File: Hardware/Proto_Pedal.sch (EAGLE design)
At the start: 124 parts, among them Q1 2.5A/30V

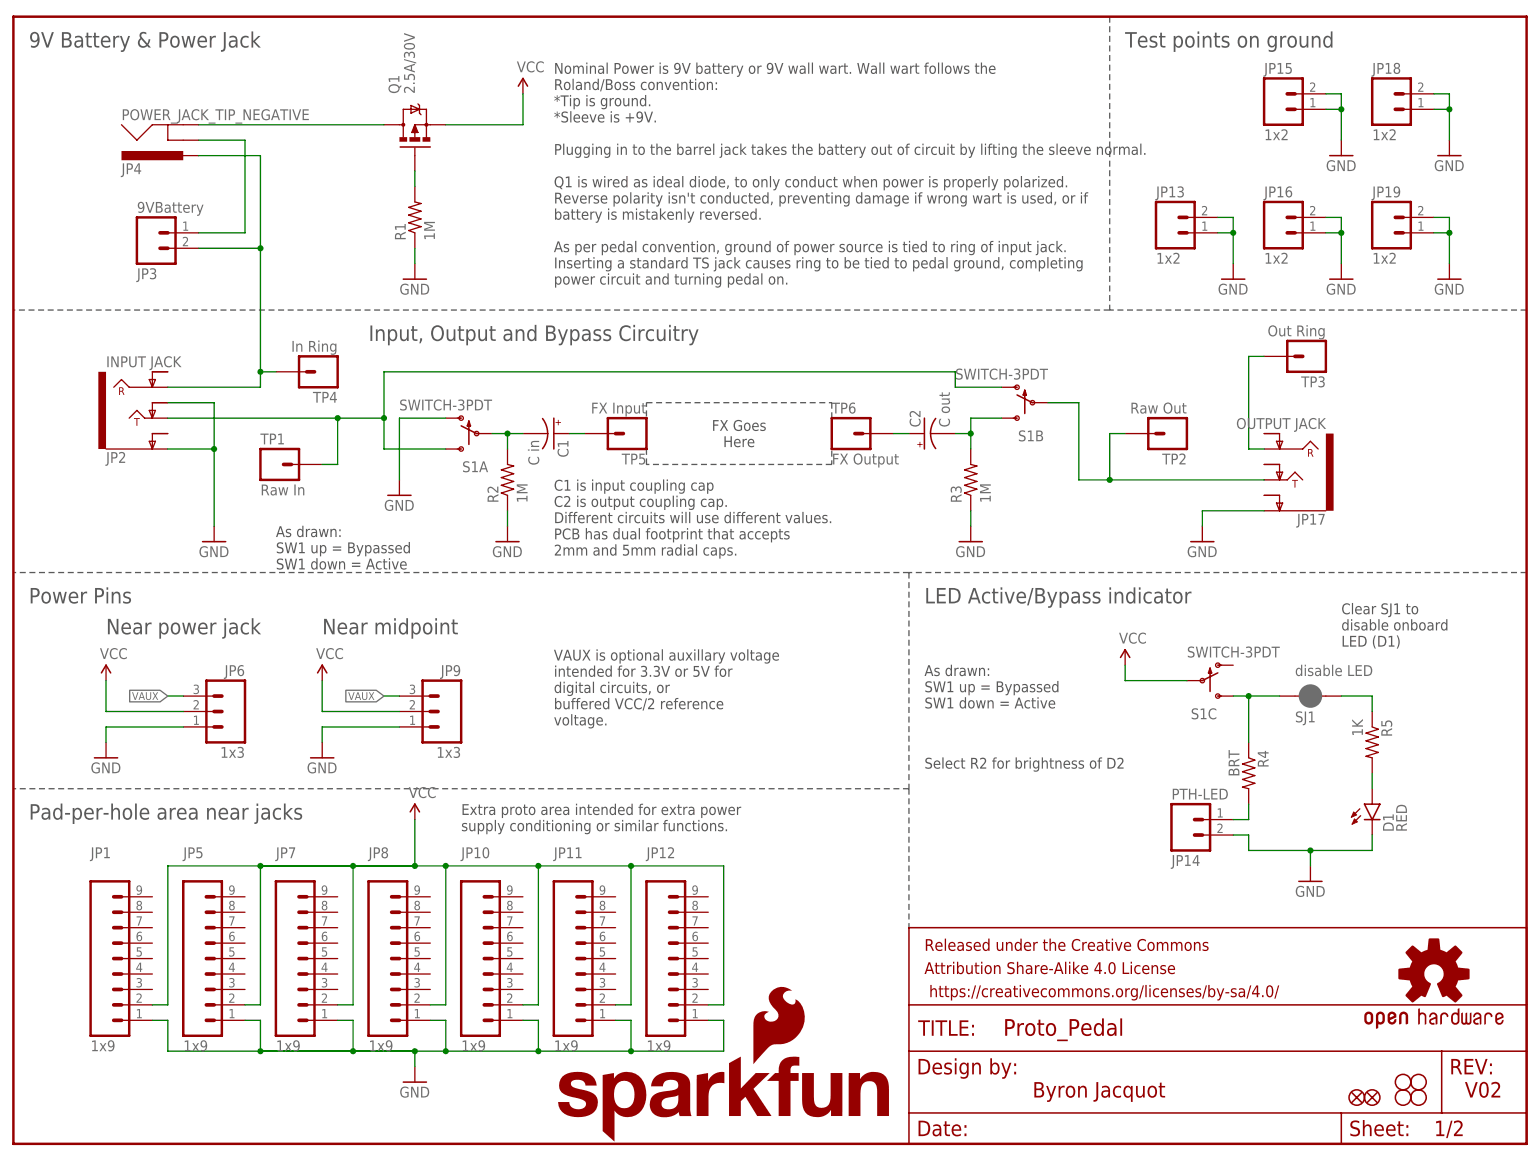
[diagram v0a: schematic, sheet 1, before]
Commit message: Updates based on proto evaluation.
Usability & fit'n'finish issues solved.
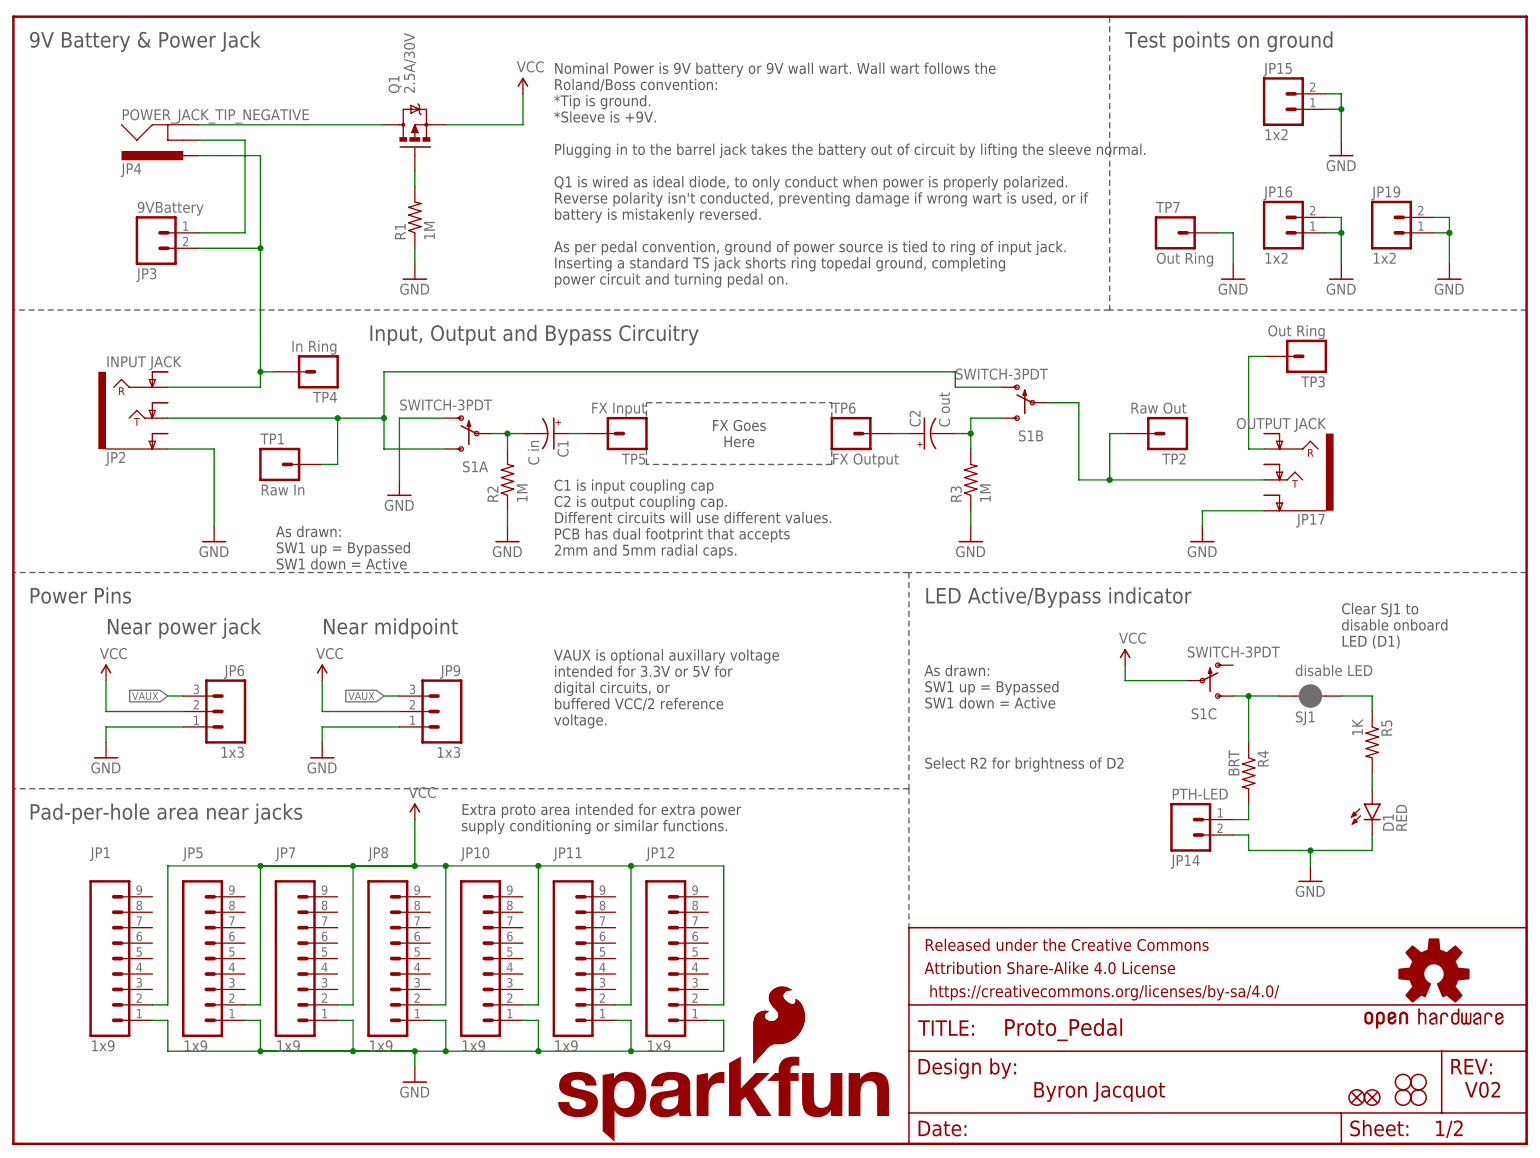
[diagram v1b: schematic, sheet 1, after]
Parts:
- removed JP13, JP18: 1x2, SparkFun-Connectors:M021X02_NO_SILK
- added LOGO3: SFE_LOGO_FLAME.2_INCH, SparkFun-Aesthetics:SFE_LOGO_FLAME.2_INCH
- added TP7: Out Ring, SparkFun-Connectors:M01PTH_NO_SILK_YES_STOP
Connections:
- net GND: now also TP7.1; no longer JP13.1, JP13.2, JP18.1, JP18.2, JP2.TIP-NORM

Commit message: PCB updates after Marshall looked closer.
A new more nits cleaned up.
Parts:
- TP7: device SparkFun-Connectors:M01PTH_NO_SILK_YES_STOP -> SparkFun-Connectors:M01PTH_LONGPAD
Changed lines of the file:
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@@
 <part name="FID1" library="SparkFun-Aesthetics" deviceset="FIDUCIAL" device="1X2"/>
 <part name="JP4" library="Testing" deviceset="POWER_JACK_TIP_NEGATIVE" device=""/>
-<part name="TP7" library="SparkFun-Connectors" deviceset="M01" device="PTH_NO_SILK_YES_STOP" value="Out Ring"/>
+<part name="TP7" library="SparkFun-Connectors" deviceset="M01" device="PTH_LONGPAD" value="Out Ring"/>
 <part name="LOGO3" library="SparkFun-Aesthetics" deviceset="SFE_LOGO_FLAME" device=".2_INCH" value="SFE_LOGO_FLAME.2_INCH"/>
 </parts>

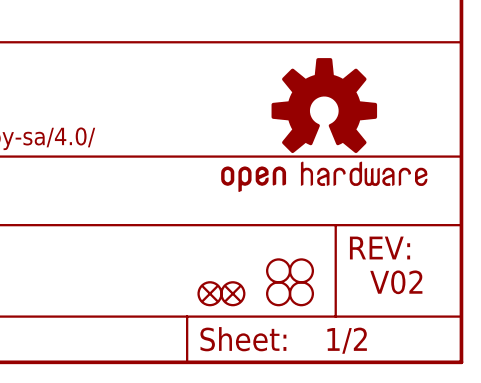
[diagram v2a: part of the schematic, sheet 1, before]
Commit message: Tweaks from checklist.
- and + signs on rails are a bit smaller.
+'s next to C1 and C2 were overlapping bare copper.
Version bumped to V03.
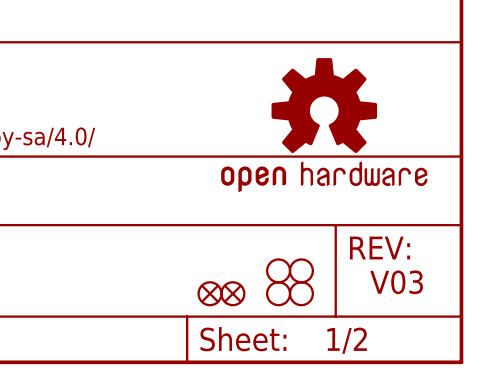
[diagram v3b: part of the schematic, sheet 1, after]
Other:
- note added: "V03"
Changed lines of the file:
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@@
 <plain>
 <text x="167.64" y="7.62" size="2.54" layer="94" font="vector">Byron Jacquot</text>
-<text x="238.76" y="7.62" size="2.54" layer="94" font="vector">V02</text>
+<text x="238.76" y="7.62" size="2.54" layer="94" font="vector">V03</text>
 <text x="2.54" y="88.9" size="2.54" layer="97">Power Pins</text>
 <text x="50.8" y="83.82" size="2.54" layer="97">Near midpoint</text>

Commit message: Silkscreen touchups from V03 proto.
Prepping for redboard review.
Rolling version to V10.
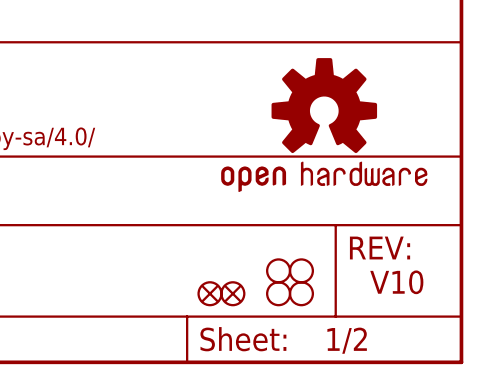
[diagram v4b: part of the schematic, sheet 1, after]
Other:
- note added: "V10"
- note removed: "V03"
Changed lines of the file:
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@@
 <?xml version="1.0" encoding="utf-8"?>
 <!DOCTYPE eagle SYSTEM "eagle.dtd">
-<eagle version="7.3.0">
+<eagle version="7.5.0">
 <drawing>
 <settings>
@@
 <plain>
 <text x="167.64" y="7.62" size="2.54" layer="94" font="vector">Byron Jacquot</text>
-<text x="238.76" y="7.62" size="2.54" layer="94" font="vector">V03</text>
+<text x="238.76" y="7.62" size="2.54" layer="94" font="vector">V10</text>
 <text x="2.54" y="88.9" size="2.54" layer="97">Power Pins</text>
 <text x="50.8" y="83.82" size="2.54" layer="97">Near midpoint</text>
